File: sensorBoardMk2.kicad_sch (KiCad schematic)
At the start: 34 parts, among them U1 SHT45, U2 BME280, U3 SGP40-D-R4, U4 IS31FL3193-DLS2-TR, U5 MCP23008-xML

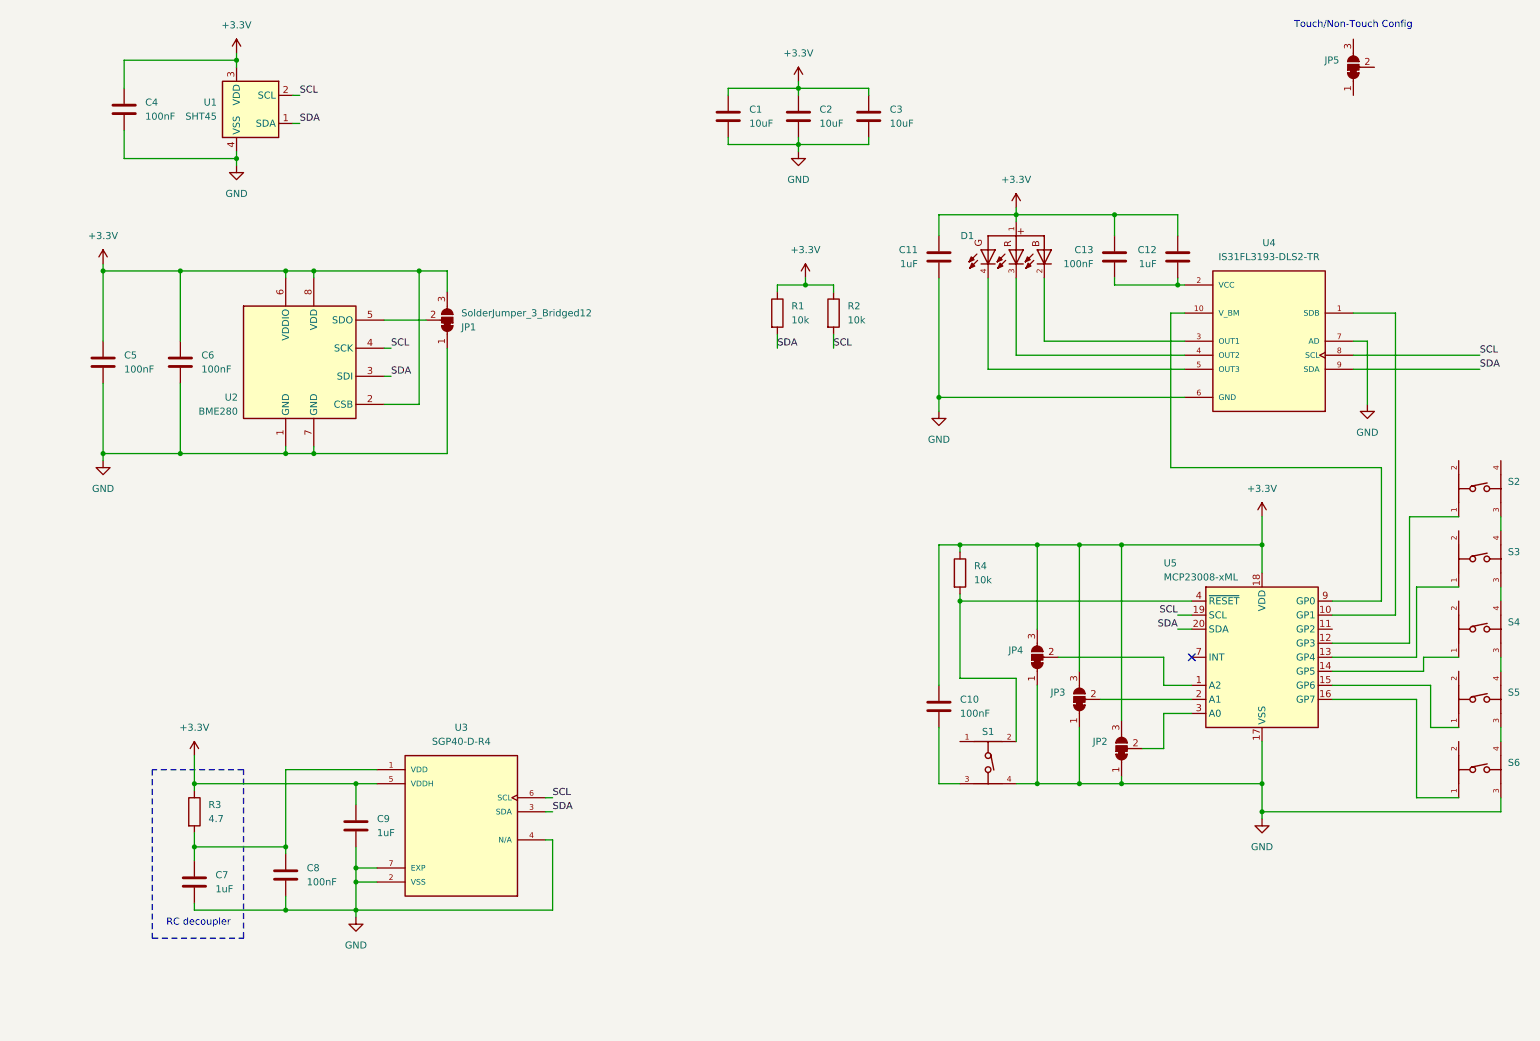
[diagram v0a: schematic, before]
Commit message: Completed first version of the schema
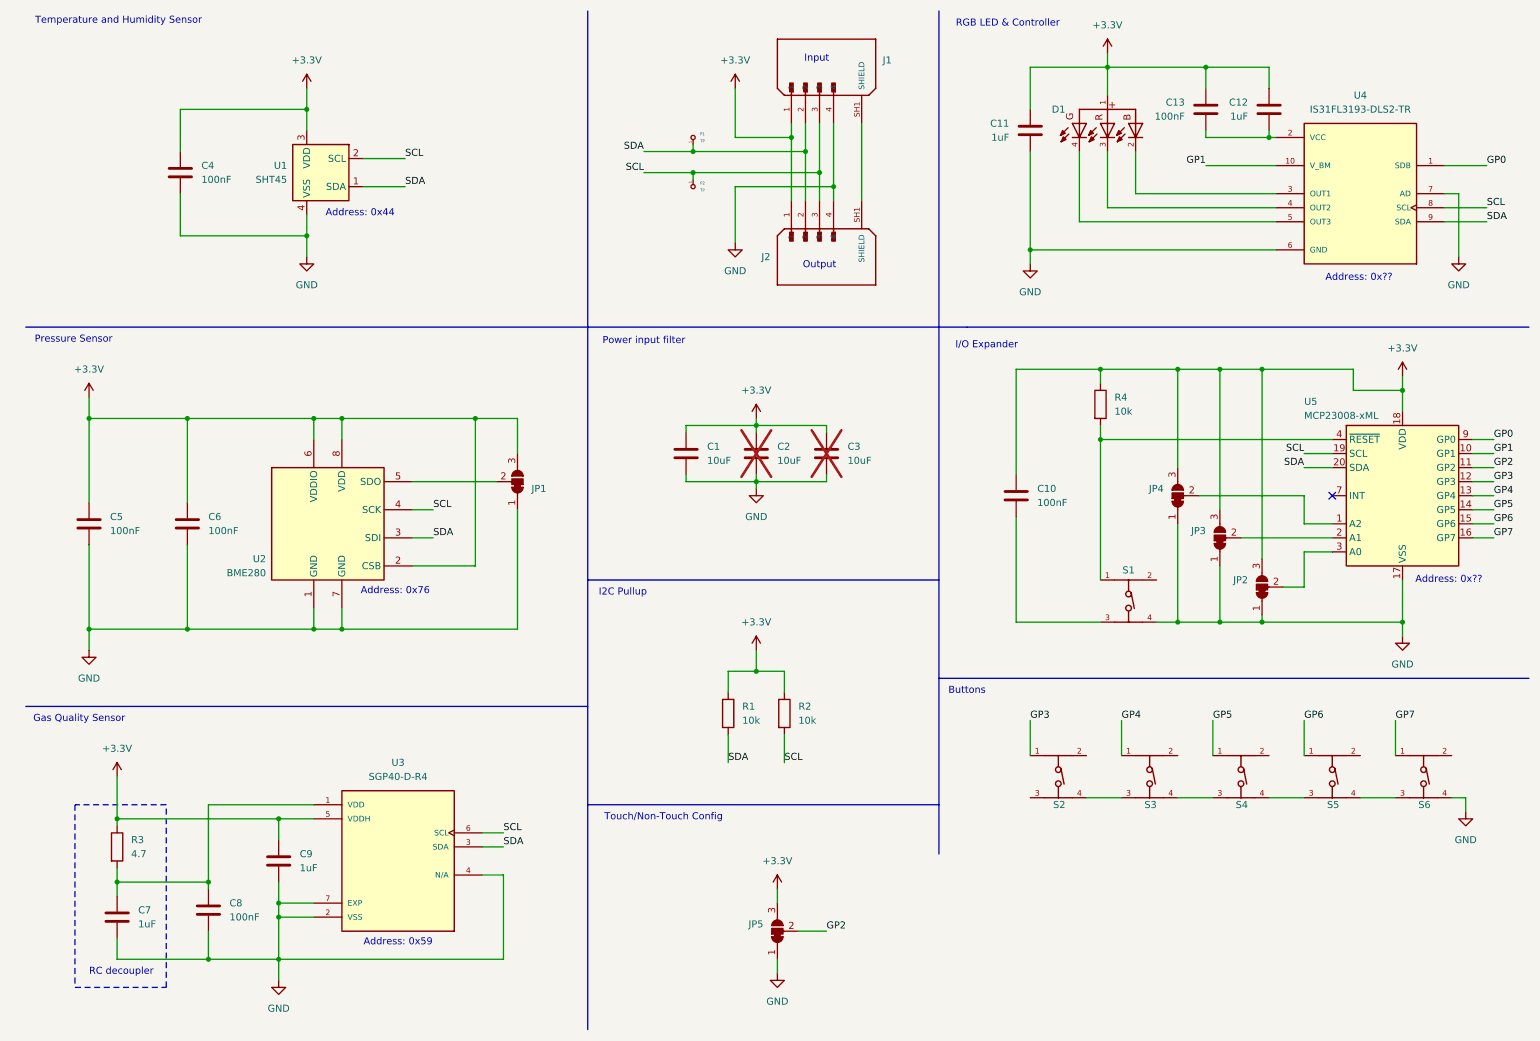
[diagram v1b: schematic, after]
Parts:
- added J1, J2: B4B-PH-SM4-TB, B4B-PH-SM4-TB:JST_B4B-PH-SM4-TB, symbol B4B-PH-SM4-TB:B4B-PH-SM4-TB
- added P1, P2: TP, symbol tinkerforge:TP
- C2, C3: now not fitted
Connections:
- net +3.3V: now also JP5.3 (B), J1.1, J2.1
- net GND: now also JP5.1 (A), S6.4, J1.4, J2.4; no longer S6.3
- net SCL: now also J1.3, J2.3, P2.1
- net SDA: now also J1.2, J2.2, P1.1
- net GP0: now reaches U4.1 (SDB)
- net GP0: now also U5.9 (GP0); no longer U5.10 (GP1)
- net GP2: now reaches U5.11 (GP2)
- net GP2: now also JP5.2 (C)
- net GP3: now reaches S2.1, U5.12 (GP3)
- net GP4: now reaches S3.1, U5.13 (GP4)
- net GP5: now reaches S4.1, U5.14 (GP5)
- net GP6: now reaches S5.1, U5.15 (GP6)
- net GP7: now reaches S6.1, U5.16 (GP7)
- net at R4.2, U5.4 (~{RESET}): now also S1.1; no longer S1.2
- net GP1: now reaches U4.10 (V_BM)
- net GP1: now also U5.10 (GP1); no longer U5.9 (GP0)
- net at S5.3: now also S4.4; no longer S6.4
- net at S5.4: now also S6.3; no longer S4.3
- net at S3.3: now also S2.4; no longer S4.4
- net at S3.4: now also S4.3; no longer S2.3
- new net: J1.SH1 (SHIELD), J1.SH2 (SHIELD), J2.SH1 (SHIELD), J2.SH2 (SHIELD)
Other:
- note added: "Address: 0x44"
- note added: "Address: 0x59"
- note added: "Address: 0x76"
- note added: "Address: 0x??"
- note added: "Buttons"
- note added: "Gas Quality Sensor"
- note added: "I/O Expander"
- note added: "I2C Pullup"
- note added: "Input"
- note added: "Output"
- note added: "Power input filter"
- note added: "Pressure Sensor"
- note added: "RGB LED & Controller"
- note added: "Temperature and Humidity Sensor"
- moved on the sheet: C1, C10, C11, C12, C13, C4, C5, C6, C7, C8, C9, D1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

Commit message: Updated Schematic: Added always power on
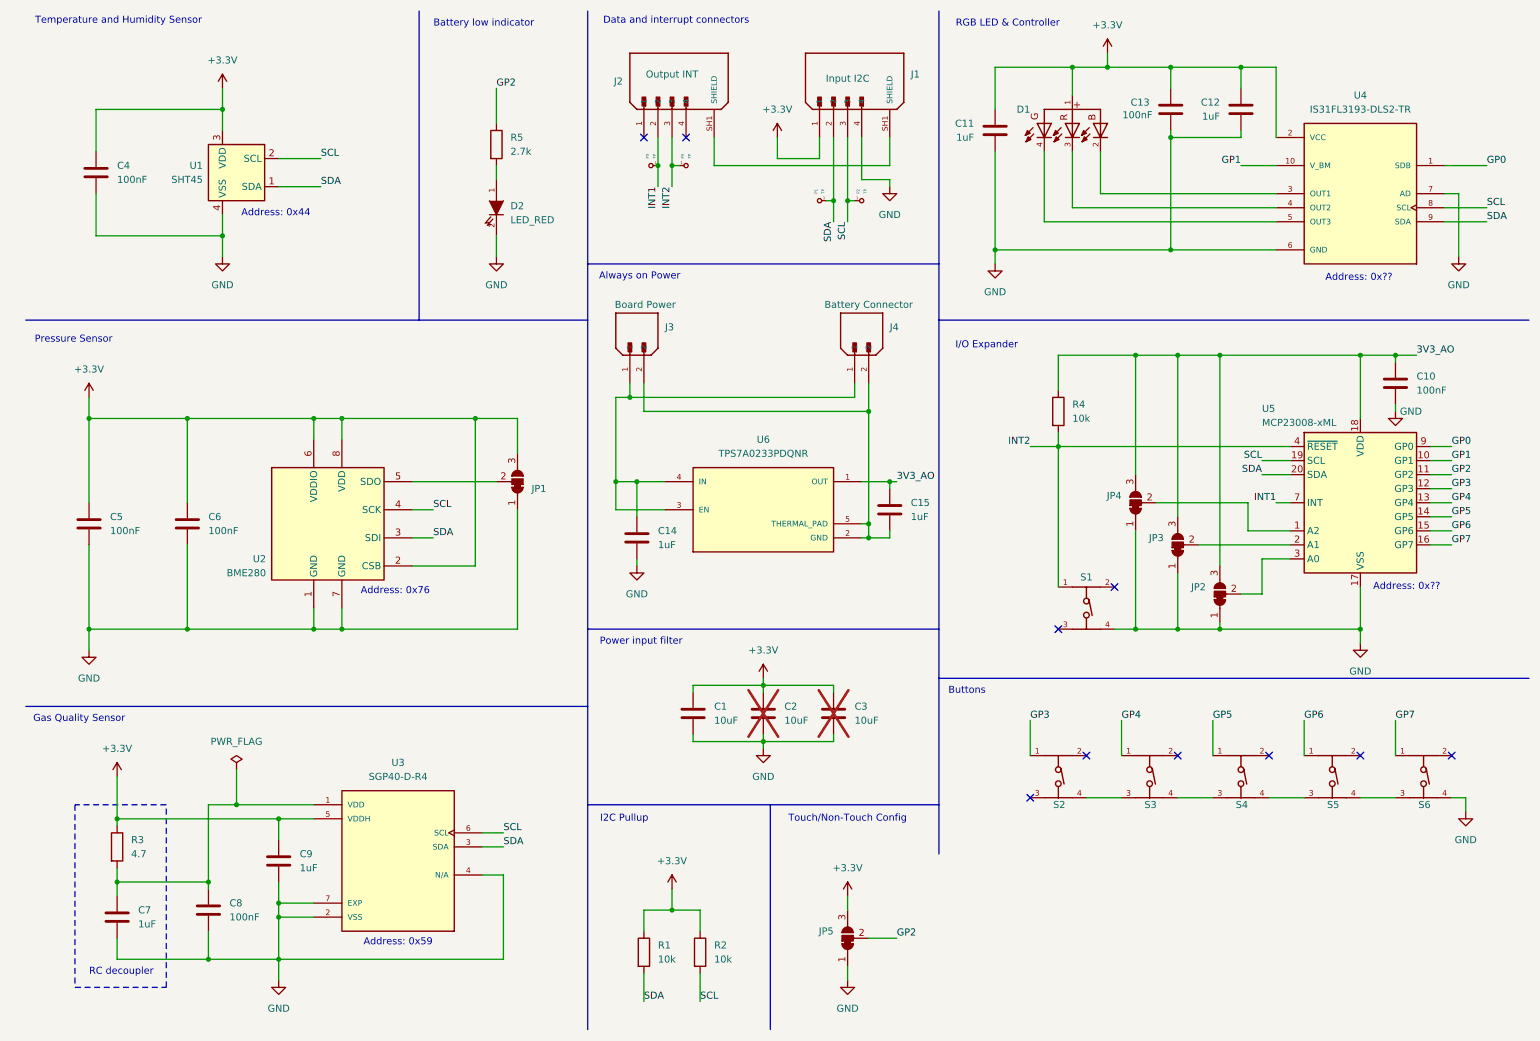
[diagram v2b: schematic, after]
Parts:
- added C14, C15: 1uF, Capacitor_SMD:C_0805_2012Metric_Pad1.18x1.45mm_HandSolder, symbol Device:C
- added D2: LED_RED, LED_SMD:LED_0805_2012Metric_Pad1.15x1.40mm_HandSolder, symbol tinkerforge:LED
- added J3, J4: B2B-PH-SM4-TB, Connector_JST:JST_PH_B2B-PH-SM4-TB_1x02-1MP_P2.00mm_Vertical, symbol B2B-PH-SM4-TB:B2B-PH-SM4-TB
- added P3, P4: TP, TestPoint:TestPoint_Pad_2.0x2.0mm, symbol tinkerforge:TP
- added R5: 2.7k, Resistor_SMD:R_0805_2012Metric_Pad1.20x1.40mm_HandSolder, symbol Device:R
- added U6: TPS7A0233PDQNR, sensorBoardMk2Library:IC_TPS7A0233PDQNR, symbol 3V3-Regulator:TPS7A0233PDQNR
- C1, C10, C11, C12, C13, C2, C3, C4, C5, C6, C7, C8, C9: footprint (none) -> Capacitor_SMD:C_0805_2012Metric_Pad1.18x1.45mm_HandSolder
- D1: footprint WL-SFTW_3528_PLCC4:WL-SFTW_3528_PLCC4 -> sensorBoardMk2Library:WL-SFTW_3528_PLCC4
- J1: footprint B4B-PH-SM4-TB:JST_B4B-PH-SM4-TB -> sensorBoardMk2Library:JST_B4B-PH-SM4-TB
- J2: footprint B4B-PH-SM4-TB:JST_B4B-PH-SM4-TB -> Connector_JST:JST_PH_B4B-PH-SM4-TB_1x04-1MP_P2.00mm_Vertical
- JP2, JP3, JP4, JP5: footprint (none) -> Jumper:SolderJumper-3_P1.3mm_Open_RoundedPad1.0x1.5mm_NumberLabels
- P1, P2: footprint (none) -> TestPoint:TestPoint_Pad_2.0x2.0mm
- R1, R2, R3, R4: footprint (none) -> Resistor_SMD:R_0805_2012Metric_Pad1.20x1.40mm_HandSolder
- S1, S2, S3, S4, S5, S6: footprint 430181038816:430181038816 -> sensorBoardMk2Library:430181038816
- U3: footprint SGP40-D-R4:XCDR_SGP40-D-R4 -> sensorBoardMk2Library:XCDR_SGP40-D-R4
- U4: footprint IS31FL3193-DLS2-TR:SON50P300X300X80-11N -> sensorBoardMk2Library:SON50P300X300X80-11N
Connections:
- net +3.3V: now also U4.2 (VCC); no longer C10.1, J2.1, JP2.3 (B), JP3.3 (B), JP4.3 (B), R4.1, U5.18 (VDD)
- net GND: now also C10.2, C12.2, C13.2, C14.2, D2.2 (K); no longer J2.4
- net GP2: now also R5.1
- net SCL: no longer J2.3
- net SDA: no longer J2.2
- net INT2: now reaches R4.2, S1.1, U5.4 (~{RESET})
- net INT2: now also J2.3, P4.1
- net INT1: now reaches U5.7 (INT)
- net INT1: now also J2.2, P3.1
- net at S1.3: no longer C10.2
- new net: C14.1, J3.1, J4.1, U6.3 (EN), U6.4 (IN)
- new net: C15.2, J3.2, J4.2, U6.2 (GND), U6.5 (THERMAL_PAD)
- new net: D2.1 (A), R5.2
- new net 3V3_AO: C10.1, C15.1, JP2.3 (B), JP3.3 (B), JP4.3 (B), R4.1, U5.18 (VDD), U6.1 (OUT)
- no-connect marks 1 -> 10
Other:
- note added: "Always on Power"
- note added: "Battery low indicator"
- note added: "Data and interrupt connectors"
- note removed: "Input"
- note removed: "Output"
- moved on the sheet: C1, C10, C11, C12, C13, C2, C3, C4, D1, J1, J2, JP2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
